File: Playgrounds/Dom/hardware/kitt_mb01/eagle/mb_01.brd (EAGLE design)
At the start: 160 x 100 mm, 19 parts, among them IC1 LA5744TP

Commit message: Board and Library Updates  - kitt.con.lbr: connectors and connector references    -> DB01 Odometry Board Connector + board outline    -> Arduino Uno shield pins + (pin) overlay for ghostcar  - kitt.ic.lbr: added battery charger component from prev. board
 - mb01.*: motherboard for scaleauto
   -> added board connectors
   -> extended board size and corrected mounting holes
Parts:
- removed SJ2, SJ3: (no value), jumper:SJ
- added CON1: ARDUINO_UNO, kitt.con:AU_PINS
- added CON2: KITT.DB01, kitt.con:KITT_DB01
- added IC2: BQ24266RGET, kitt.ic:VQFN-24
- added REF4: REF_GC-BBV2.0, kitt.con:REF_GHOSTCAR
- added SJ4, SJ5, SJ6: (no value), jumper:SJ
- added TP1, TP2: TPSQTP19SQ, testpad:TP19SQ
- L1.01: value (none) -> 22uH
- moved L2 62.5 mm to (112.2, 58.6), turned to 0 degrees
- moved C2 54.9 mm to (108.5, 56.1), turned to 180 degrees
- moved C1.03 50.8 mm to (103.7, 56.1), turned to 0 degrees
- moved D2 49.5 mm to (109.4, 51.7), turned to 180 degrees
- moved SJ1 44.3 mm to (114.6, 33.3)
- moved F1 40.9 mm to (112.0, 38.7), turned to 180 degrees
- moved L1.01 39.8 mm to (110.1, 44.9)
- moved C1 37.6 mm to (102.6, 45.0), turned to 180 degrees
- moved IC1 37.3 mm to (96.1, 49.8), turned to 90 degrees
- moved R1.02 37.2 mm to (103.5, 58.3), turned to 0 degrees
- moved X1 36.1 mm to (115.0, 28.9), turned to 90 degrees
- moved L1 34.3 mm to (104.4, 40.2), turned to 90 degrees
- moved D1 33.5 mm to (108.8, 30.2)
- moved R1.01 33.4 mm to (99.0, 58.3), turned to 0 degrees
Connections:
- net GND: now also CON1.GND2, CON1.GND3, CON2.10, CON2.6, CON2.8, IC2.20, IC2.22, IC2.PAD, SJ4.1, SJ5.1, SJ6.1; no longer SJ2.2, SJ3.2
- net GNDA: no longer SJ2.1, SJ3.1
- net N$4: now also TP1.TP
- net N$5: now also TP2.TP
- net THERM.1: now also SJ4.2, SJ5.2, SJ6.2
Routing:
- net GND: track 0.00 -> 83.2 mm
- net N$5: track 0.00 -> 25.3 mm
- net N$7: track 0.00 -> 17.3 mm
- net THERM.1: track 0.00 -> 15.8 mm
- net N$4: track 0.00 -> 12.1 mm
- net +12V: track 0.00 -> 8.39 mm
- net VCC/2: track 0.00 -> 6.69 mm
- net N$3: track 0.00 -> 6.38 mm
- net N$2: track 0.00 -> 5.36 mm
- net GNDA: track 0.00 -> 3.99 mm
- net N$1: track 0.00 -> 3.92 mm
- added copper zone on layer 1, net THERM.1
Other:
- outline, holes or cut-outs redrawn
- board text added: "<-- Rail Power Leads"
- board text added: "Motor Leads -->"

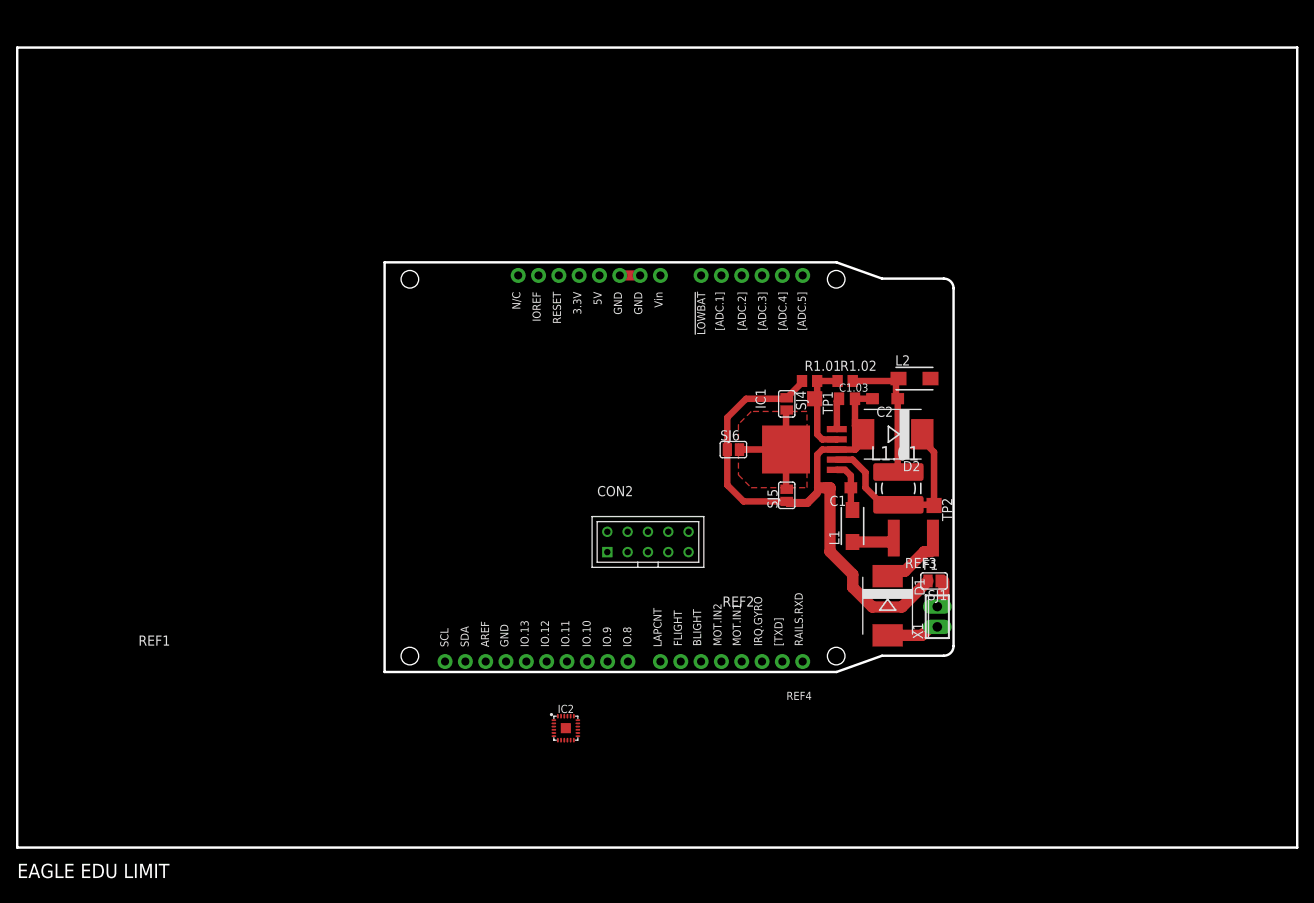
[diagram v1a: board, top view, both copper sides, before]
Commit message: entered the charging circuit
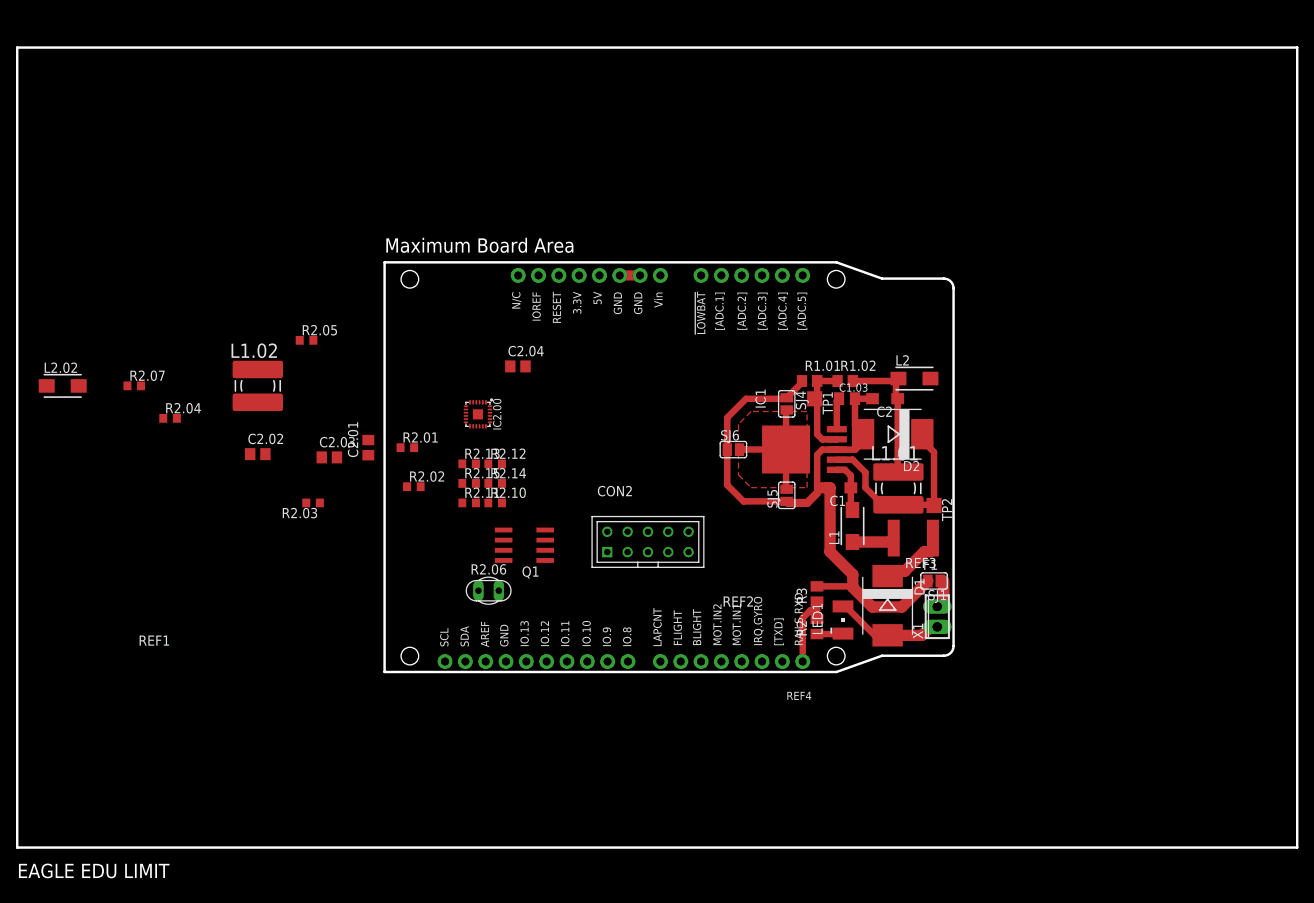
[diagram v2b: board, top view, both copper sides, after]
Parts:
- removed IC2: BQ24266RGET, kitt.ic:VQFN-24
- added C2.01: 1uF/16V, rcl:C0805
- added C2.02: 2.2uF/10V, rcl:C0805
- added C2.03, C2.04: 33nF/16V, rcl:C0805
- added IC2.00: BQ24266RGET, kitt.ic:VQFN-24
- added L1.02: 2.6uH, rcl:POWER-CHOKE_WE-TPC
- added L2.02: BEAD, inductor-neosid:SM-B5
- added LED1: (no value), led:PLCC2
- added Q1: (no value), transistor-power:SO-08
- added R2: 10kR, rcl:M0805
- added R2.01, R2.10, R2.11, R2.12, R2.13, R2.14, R2.15: 10kR, rcl:R0603
- added R2.02: 31k6R, rcl:R0603
- added R2.03: 1k62R, rcl:R0603
- added R2.04: 5k62R, rcl:R0603
- added R2.05: 11k8R, rcl:R0603
- added R2.06: 10kR/NTC, ptc-ntc:P642
- added R2.07: 0R, rcl:R0603
- added R3: 2k2R, rcl:M0805
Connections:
- new net +4.1V: L2.02.2, R2.04.1, R2.10.2, R2.12.2, R2.14.2
- new net IC2.0.!CHG: IC2.00.13
- new net IC2.0.!PG: IC2.00.10
- new net N$10: LED1.C, R2.1
- new net N$11: IC2.00.15, R2.01.2, R2.02.1
- new net N$12: C2.03.1, IC2.00.23, IC2.00.24, L1.02.2
- new net N$13: C2.03.2, IC2.00.2
- new net N$14: IC2.00.11, Q1.4
- new net N$15: IC2.00.5, R2.04.2, R2.05.1, R2.06.2
- new net N$16: L2.02.1, R2.07.1
- new net N$17: IC2.00.8, IC2.00.9, Q1.5, Q1.6, Q1.7, Q1.8
- new net N$18: C2.04.1, IC2.00.6, IC2.00.7, L1.02.1, Q1.1, Q1.2, Q1.3, R2.07.2
- new net N$19: IC2.00.12, R2.03.2
- new net N$20: IC2.00.17, R2.10.1, R2.11.2
- new net N$21: IC2.00.16, R2.12.1, R2.13.2
- new net N$22: IC2.00.14, R2.14.1, R2.15.2
- new net N$8: C2.01.1, IC2.00.1
- new net N$9: IC2.00.18, IC2.00.19, R2.02.2
- new net RAILS.RX: CON1.IO.0, R2.2, R3.1
- new net V+: C2.02.1, IC2.00.3
- net GND: now also C2.01.2, C2.02.2, C2.04.2, IC2.00.20, IC2.00.21, IC2.00.22, IC2.00.PAD, R2.01.1, R2.03.1, R2.05.2, R2.06.1, R2.11.1, R2.13.1, R2.15.1, R3.2; no longer IC2.20, IC2.22, IC2.PAD
- net VCC/2: now also LED1.A
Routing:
- net RAILS.RX: track 0.00 -> 9.80 mm
- net VCC/2: track 6.69 -> 13.9 mm
- net GND: track 83.2 -> 87.7 mm
- net N$10: track 0.00 -> 3.28 mm
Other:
- board text added: "Maximum Board Area"

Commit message: started copying the layout surrounding the battery charger from the previous version imported bottom copper reference seems to be not quite to scale, but no worries
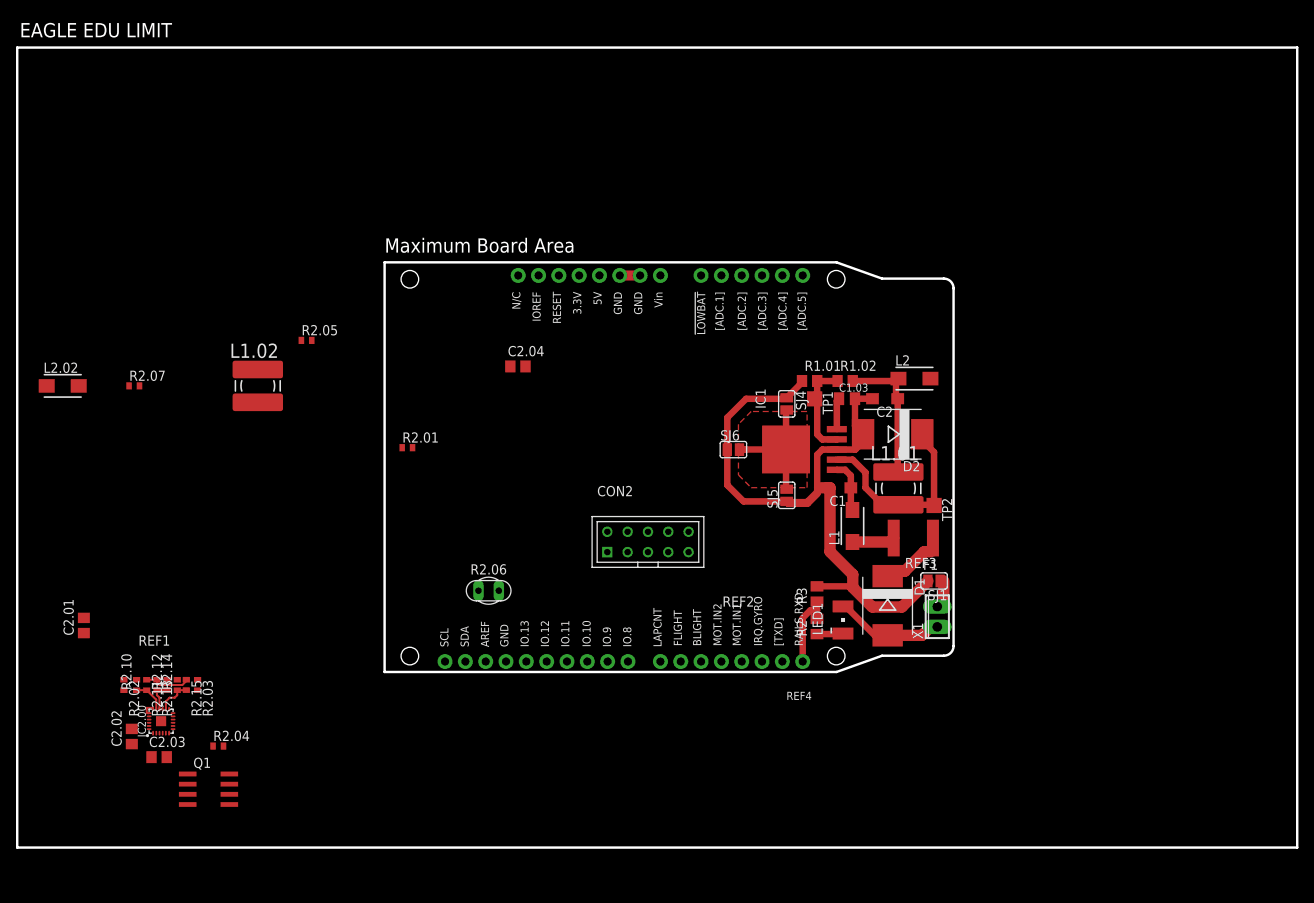
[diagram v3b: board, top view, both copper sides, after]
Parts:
- added REF5: REF.GHOSTCAR.BCP, kitt.refs:REF_GCB2_BS
- R2.01, R2.02, R2.03, R2.04, R2.05, R2.07, R2.10, R2.11, R2.12, R2.13, R2.14, R2.15: device rcl:R0603 -> rcl:R0402
- moved IC2.00 55.1 mm to (18.0, 15.8), turned to 90 degrees
- moved R2.10 50.3 mm to (14.9, 20.3), turned to 90 degrees
- moved Q1 49.9 mm to (23.9, 7.29), turned to 270 degrees
- moved R2.12 49.5 mm to (18.7, 20.3), turned to 90 degrees
- moved R2.13 47.8 mm to (17.5, 20.3), turned to 270 degrees
- moved R2.14 47.1 mm to (20.0, 20.3), turned to 90 degrees
- moved R2.11 46.3 mm to (16.2, 20.3), turned to 270 degrees
- moved R2.02 43.9 mm to (13.3, 20.3), turned to 270 degrees
- moved R2.15 43.4 mm to (21.1, 20.3), turned to 270 degrees
- moved C2.03 43.1 mm to (17.7, 11.3)
- moved C2.01 41.9 mm to (8.33, 27.8)
- moved R2.04 41.4 mm to (25.1, 12.7)
- moved C2.02 38.6 mm to (14.3, 13.9), turned to 90 degrees
- moved R2.03 27.0 mm to (22.5, 20.3), turned to 270 degrees
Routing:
- net GND: track 87.7 -> 93.5 mm
- net N$22: track 0.00 -> 4.47 mm
- net N$20: track 0.00 -> 4.13 mm
- net N$21: track 0.00 -> 3.77 mm
- net N$9: track 0.00 -> 1.91 mm

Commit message: did some more work on copying the charger layout
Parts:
- added C2.05: 22uF, rcl:A/3216-18R
- C2.03: device rcl:C0805 -> rcl:C0603
- L2.02: device inductor-neosid:SM-B5 -> rcl:L2012C
- moved C2.04 60.2 mm to (23.2, 14.6)
- moved R2.05 54.4 mm to (21.6, 11.0), turned to 180 degrees
- moved L1.02 51.4 mm to (16.3, 8.19), turned to 270 degrees
- moved R2.07 45.1 mm to (31.0, 15.7)
- moved L2.02 44.1 mm to (28.7, 20.0), turned to 270 degrees
- moved R2.01 40.7 mm to (21.0, 20.3), turned to 270 degrees
- moved R2.06 31.4 mm to (35.6, 11.1), turned to 270 degrees
- moved C2.01 14.0 mm to (12.5, 14.4)
- moved C2.02 7.86 mm to (22.1, 12.5), turned to 0 degrees
- moved R2.02 6.51 mm to (19.8, 20.3), turned to 90 degrees
- moved C2.03 3.52 mm to (14.8, 13.2), turned to 90 degrees
- moved R2.15 2.06 mm to (23.2, 20.3)
- moved R2.14 2.06 mm to (22.1, 20.3)
- moved R2.03 1.91 mm to (24.4, 20.3)
- moved R2.04 1.75 mm to (24.9, 11.0), turned to 180 degrees
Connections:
- removed net N$17: IC2.00.8, IC2.00.9, Q1.5, Q1.6, Q1.7, Q1.8
- net +4.1V: now also C2.05.+, IC2.00.8, IC2.00.9, Q1.5, Q1.6, Q1.7, Q1.8
- net GND: now also C2.05.-
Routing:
- net N$18: track 0.00 -> 15.7 mm
- net N$8: track 0.00 -> 12.6 mm, vias 0 -> 4
- net GND: track 93.5 -> 105.4 mm
- net N$12: track 0.00 -> 9.32 mm
- net N$13: track 0.00 -> 9.04 mm, vias 0 -> 2
- net +4.1V: track 0.00 -> 7.71 mm
- net N$19: track 0.00 -> 6.69 mm
- net N$11: track 0.00 -> 4.64 mm
- net V+: track 0.00 -> 4.63 mm
- net N$22: track 4.47 -> 6.35 mm

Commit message: finished up on the charger circuit, roughly...
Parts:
- removed REF5: REF.GHOSTCAR.BCP, kitt.refs:REF_GCB2_BS
- added R2.08: [10kR/NTC], rcl:R0402
- moved C2.01 81.7 mm to (86.2, 49.5), turned to 270 degrees
- moved L1.02 81.6 mm to (82.3, 56.1), turned to 90 degrees
- moved C2.03 78.6 mm to (83.8, 50.8), turned to 270 degrees
- moved R2.10 72.6 mm to (83.7, 43.8), turned to 270 degrees
- moved Q1 71.0 mm to (74.7, 57.0), turned to 90 degrees
- moved IC2.00 70.5 mm to (80.6, 48.2), turned to 270 degrees
- moved R2.11 70.2 mm to (82.4, 43.8), turned to 90 degrees
- moved R2.05 67.9 mm to (74.8, 53.2), turned to 0 degrees
- moved R2.13 67.9 mm to (81.1, 43.8), turned to 90 degrees
- moved C2.02 65.5 mm to (74.8, 51.4), turned to 180 degrees
- moved R2.12 65.5 mm to (79.9, 43.8), turned to 270 degrees
- moved R2.02 63.4 mm to (78.7, 43.8), turned to 270 degrees
- moved C2.04 62.2 mm to (74.8, 49.4), turned to 180 degrees
- moved R2.01 61.4 mm to (77.6, 43.8), turned to 90 degrees
- moved R2.04 61.1 mm to (70.2, 52.1)
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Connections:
- net +4.1V: now also R2.07.1; no longer L2.02.2
- net GND: now also R2.08.2
- net N$15: now also R2.08.1
- net N$16: now also L2.02.2, R2.07.2; no longer L2.02.1, R2.07.1
- net N$18: now also L2.02.1; no longer R2.07.2
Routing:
- net GND: track 105.4 -> 130.1 mm, vias 0 -> 1
- net N$15: track 0.00 -> 23.0 mm, vias 0 -> 2
- net N$18: track 15.7 -> 36.3 mm, vias 0 -> 6
- net +4.1V: track 7.71 -> 24.6 mm
- net N$14: track 0.00 -> 16.3 mm, vias 0 -> 2
- net V+: track 4.63 -> 7.17 mm
- net N$16: track 0.00 -> 1.64 mm
- net N$13: track 9.04 -> 9.94 mm
